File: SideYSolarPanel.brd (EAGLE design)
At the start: 81.7 x 102 mm, 33 parts

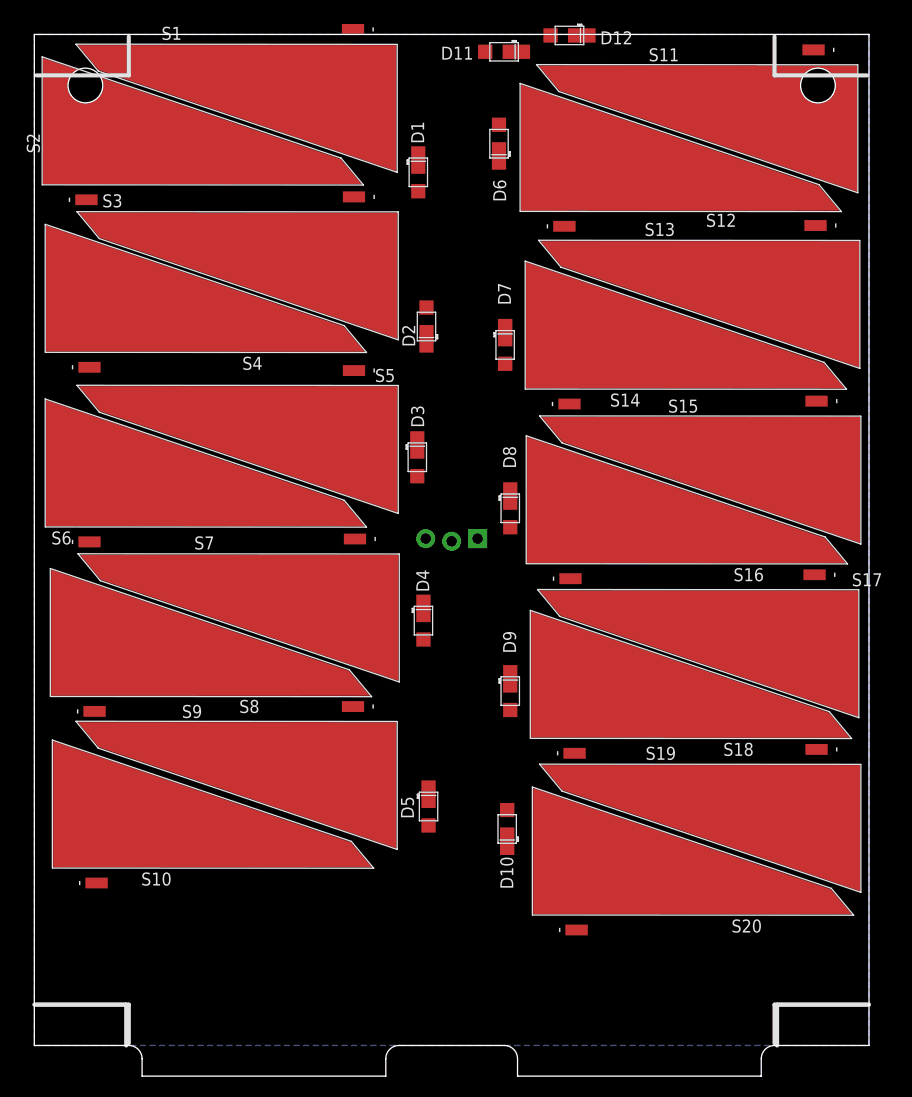
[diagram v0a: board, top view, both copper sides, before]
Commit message: Finished routing Y solar panel
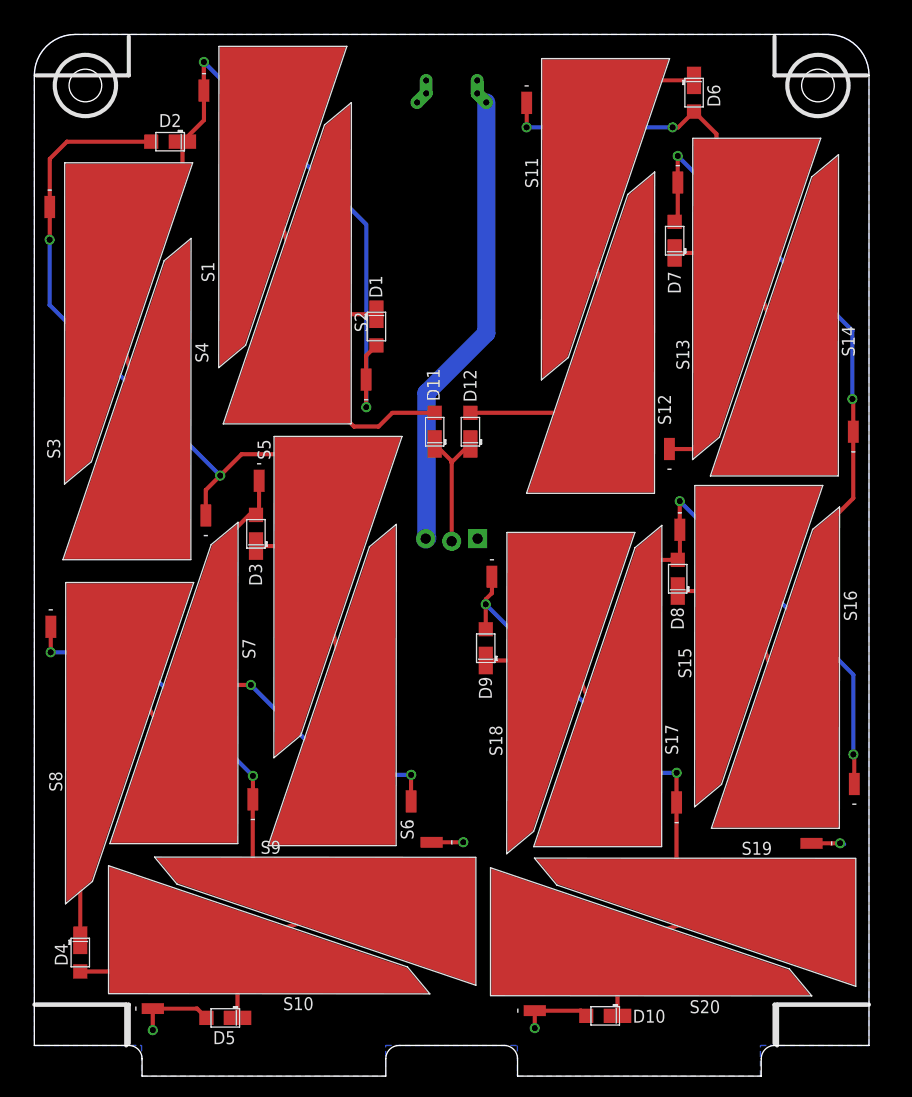
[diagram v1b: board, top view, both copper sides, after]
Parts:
- added U$1, U$2: BURNER, Burner:BURNER
- moved D4 46.7 mm to (4.50, 9.10)
- moved D12 40.0 mm to (42.7, 60.1), turned to 90 degrees
- moved D11 37.8 mm to (39.2, 60.1), turned to 90 degrees
- moved S6 36.1 mm to (35.3, 26.9), turned to 180 degrees
- moved D2 30.9 mm to (13.3, 88.5), turned to 180 degrees
- moved S16 29.8 mm to (78.7, 28.6), turned to 180 degrees
- moved D5 28.7 mm to (18.7, 2.70), turned to 180 degrees
- moved S2 28.0 mm to (30.9, 68.2), turned to 180 degrees
- moved S3 25.3 mm to (3.10, 79.1), turned to 0 degrees
- moved S11 24.4 mm to (49.8, 89.3), turned to 0 degrees
- moved S14 23.2 mm to (78.6, 63.1), turned to 180 degrees
- moved S7 22.6 mm to (19.8, 27.1), turned to 180 degrees
- moved S17 21.4 mm to (61.3, 26.8), turned to 180 degrees
- moved S12 21.2 mm to (60.6, 61.4), turned to 180 degrees
- moved D10 20.7 mm to (55.9, 2.90), turned to 180 degrees
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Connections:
- new net V_BURN: JP1.3, U$1.H1, U$1.H2, U$1.H3
- net GND: now also U$2.H1, U$2.H2, U$2.H3
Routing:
- net N$39: track 0.00 -> 119.4 mm, vias 0 -> 2
- net N$7: track 0.00 -> 107.4 mm, vias 0 -> 2
- net N$37: track 0.00 -> 103.9 mm, vias 0 -> 2
- net N$45: track 0.00 -> 103.4 mm, vias 0 -> 2
- net N$36: track 0.00 -> 97.9 mm, vias 0 -> 2
- net N$50: track 0.00 -> 96.5 mm, vias 0 -> 2
- net N$41: track 0.00 -> 86.1 mm, vias 0 -> 2
- net N$1: track 0.00 -> 86.0 mm, vias 0 -> 2
- net N$5: track 0.00 -> 66.1 mm
- net N$9: track 0.00 -> 53.3 mm
- net V_BURN: track 0.00 -> 45.2 mm
- net GND: track 0.00 -> 21.9 mm, vias 0 -> 4
- net V_SOLAR: track 0.00 -> 12.8 mm
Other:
- outline, holes or cut-outs redrawn

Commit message: Increased cutout line width
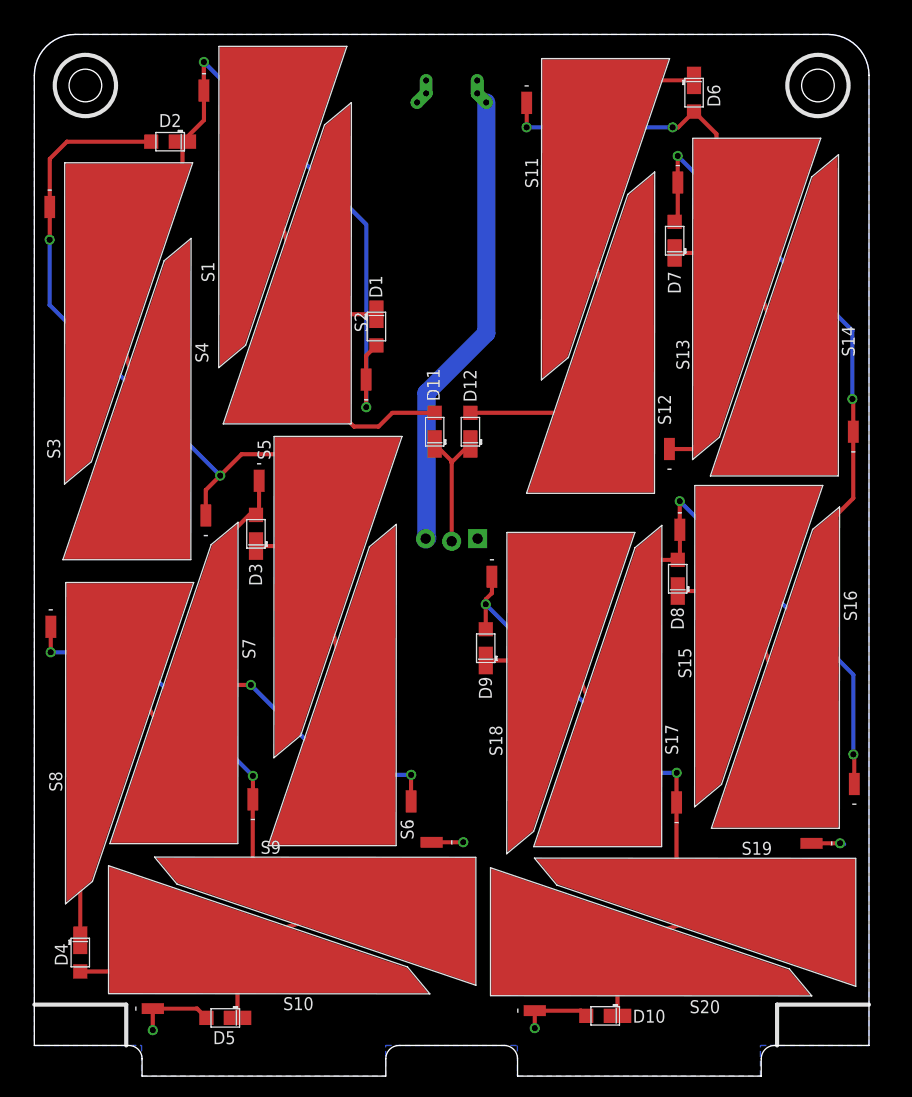
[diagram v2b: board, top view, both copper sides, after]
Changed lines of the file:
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@@
 <layer number="42" name="bRestrict" color="1" fill="10" visible="no" active="yes"/>
 <layer number="43" name="vRestrict" color="2" fill="10" visible="no" active="yes"/>
-<layer number="44" name="Drills" color="7" fill="1" visible="yes" active="yes"/>
-<layer number="45" name="Holes" color="7" fill="1" visible="yes" active="yes"/>
+<layer number="44" name="Drills" color="7" fill="1" visible="no" active="yes"/>
+<layer number="45" name="Holes" color="7" fill="1" visible="no" active="yes"/>
 <layer number="46" name="Milling" color="3" fill="1" visible="no" active="yes"/>
 <layer number="47" name="Measures" color="7" fill="1" visible="no" active="yes"/>
@@
 <layer number="113" name="IDFDebug" color="4" fill="1" visible="no" active="yes"/>
 <layer number="116" name="Patch_BOT" color="9" fill="4" visible="no" active="yes"/>
-<layer number="121" name="_tsilk" color="7" fill="1" visible="no" active="yes"/>
-<layer number="122" name="_bsilk" color="7" fill="1" visible="no" active="yes"/>
+<layer number="121" name="_tsilk" color="7" fill="1" visible="yes" active="yes"/>
+<layer number="122" name="_bsilk" color="7" fill="1" visible="yes" active="yes"/>
 <layer number="123" name="tTestmark" color="7" fill="1" visible="no" active="yes"/>
 <layer number="124" name="bTestmark" color="7" fill="1" visible="no" active="yes"/>
@@
 <wire x1="46.015" y1="0" x2="47.315" y2="-1.3" width="0" layer="20" curve="-90"/>
 <wire x1="71.18" y1="-1.3" x2="72.48" y2="0" width="0" layer="20" curve="-90"/>
-<wire x1="0.2" y1="4" x2="9.25" y2="4" width="0.4" layer="121"/>
-<wire x1="9.25" y1="4" x2="9.25" y2="0.2" width="0.4" layer="121"/>
-<wire x1="81.53" y1="94.99" x2="72.48" y2="94.99" width="0.4" layer="121"/>
-<wire x1="72.48" y1="94.99" x2="72.48" y2="98.79" width="0.4" layer="121"/>
-<wire x1="0.2" y1="94.99" x2="9.25" y2="94.99" width="0.4" layer="121"/>
-<wire x1="9.25" y1="94.99" x2="9.25" y2="98.79" width="0.4" layer="121"/>
-<wire x1="81.53" y1="4" x2="72.48" y2="4" width="0.4" layer="121"/>
-<wire x1="72.48" y1="4" x2="72.48" y2="0.2" width="0.4" layer="121"/>
-<rectangle x1="13.1" y1="58.8" x2="28.9" y2="77.8" layer="122"/>
 <hole x="5" y="94" drill="3.2"/>
 <hole x="76.73" y="94" drill="3.2"/>

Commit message: Swapped X and Y solar panels per NanoRacks ICD
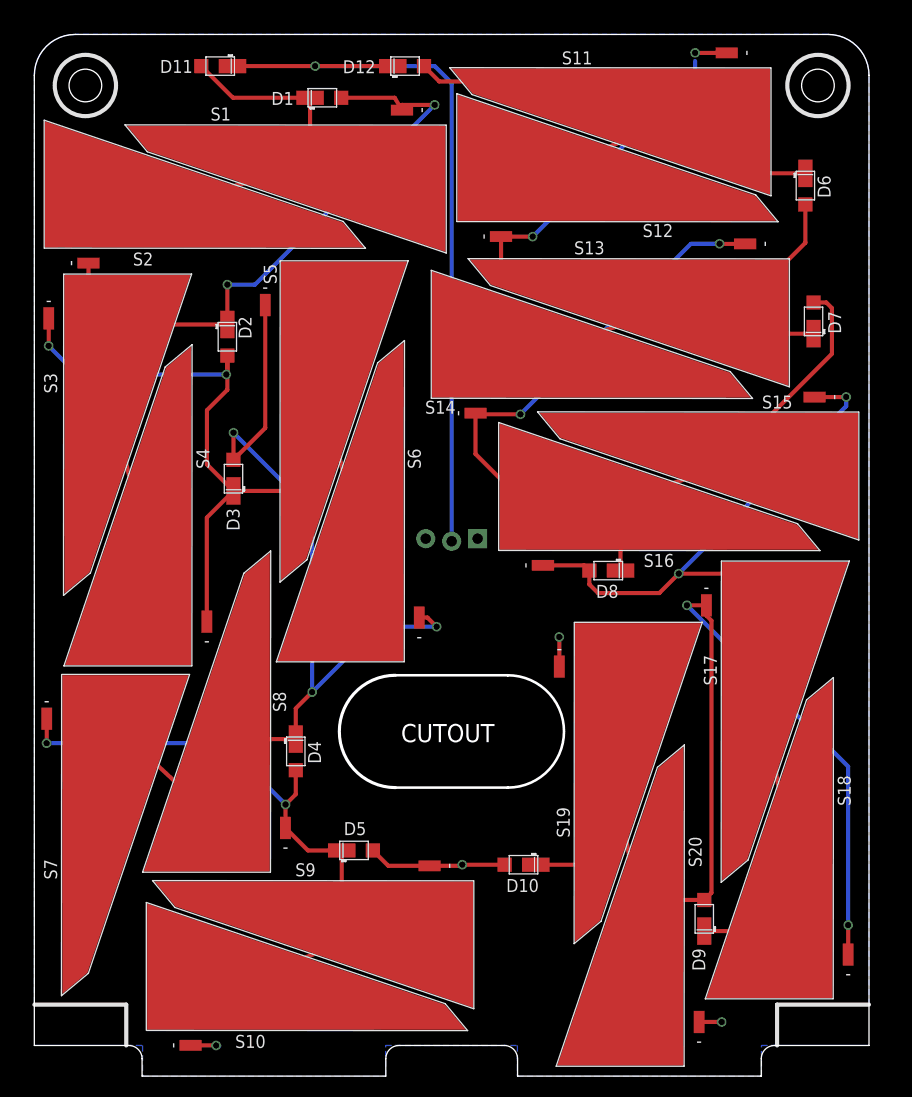
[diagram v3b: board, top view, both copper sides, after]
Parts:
- removed U$1, U$2: BURNER, Burner:BURNER
- moved S18 44.3 mm to (78.1, 11.9), turned to 180 degrees
- moved D11 41.5 mm to (18.2, 95.9), turned to 180 degrees
- moved D12 36.4 mm to (36.3, 95.9), turned to 0 degrees
- moved D9 34.1 mm to (65.6, 12.4)
- moved S16 32.7 mm to (52.8, 48.6), turned to 90 degrees
- moved S14 32.4 mm to (46.2, 63.5), turned to 90 degrees
- moved D4 28.9 mm to (25.6, 28.8)
- moved S19 25.6 mm to (53.0, 34.1), turned to 0 degrees
- moved S2 24.7 mm to (8.30, 78.2), turned to 90 degrees
- moved S8 24.1 mm to (23.0, 24.3), turned to 180 degrees
- moved D1 23.0 mm to (28.2, 92.8), turned to 0 degrees
- moved S12 22.8 mm to (48.7, 80.8), turned to 90 degrees
- moved D5 20.7 mm to (31.3, 19.1), turned to 0 degrees
- moved D2 19.9 mm to (18.9, 69.4), turned to 270 degrees
- moved S6 18.0 mm to (36.1, 44.9)
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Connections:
- removed net V_BURN: JP1.3, U$1.H1, U$1.H2, U$1.H3
- net GND: no longer U$2.H1, U$2.H2, U$2.H3
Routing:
- net V_SOLAR: track 12.8 -> 74.6 mm, vias 0 -> 1
- net V_BURN: track 45.2 -> 0.00 mm
- net N$41: track 86.1 -> 128.2 mm
- net N$50: track 96.5 -> 79.2 mm
- net N$39: track 119.4 -> 104.1 mm, vias 2 -> 3
- net N$1: track 86.0 -> 97.7 mm
- net N$5: track 66.1 -> 76.4 mm
- net N$45: track 103.4 -> 95.6 mm
- net N$37: track 103.9 -> 99.6 mm
- net N$9: track 53.3 -> 54.5 mm
- net N$7: track 107.4 -> 108.5 mm
- net GND: track 21.9 -> 22.9 mm
- net N$36: track 97.9 -> 98.5 mm
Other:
- outline, holes or cut-outs redrawn
- board text added: "CUTOUT"

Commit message: Cleanup
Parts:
- added FRAME1: FRAME-LETTER, SparkFun-Aesthetics:CREATIVE_COMMONS
- added U$1: KICKSAT_LOGO, KickSat-Logo:KICKSAT_LOGO
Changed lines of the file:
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@@
 </element>
 <element name="JP1" library="SparkFun-Connectors" package="MOLEX-1X3_LOCK" value="" x="43.405" y="49.5" rot="MR0"/>
+<element name="FRAME1" library="SparkFun-Aesthetics" package="CREATIVE_COMMONS" value="FRAME-LETTER" x="20.8" y="-10.6"/>
+<element name="U$1" library="KickSat-Logo" package="KICKSAT_LOGO" value="KICKSAT_LOGO" x="54.2" y="2.8" rot="MR0"/>
 </elements>
 <signals>

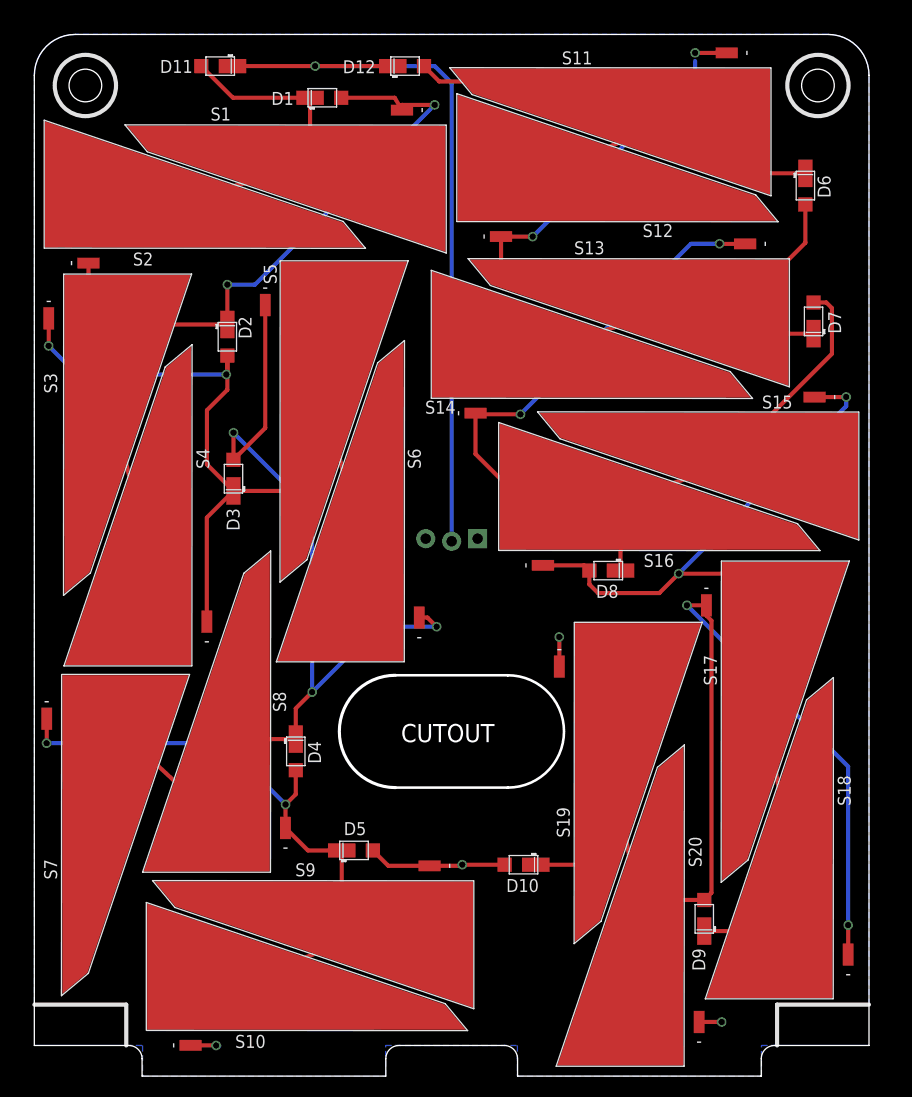
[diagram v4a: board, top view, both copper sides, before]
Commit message: Fixed solar cell footprints
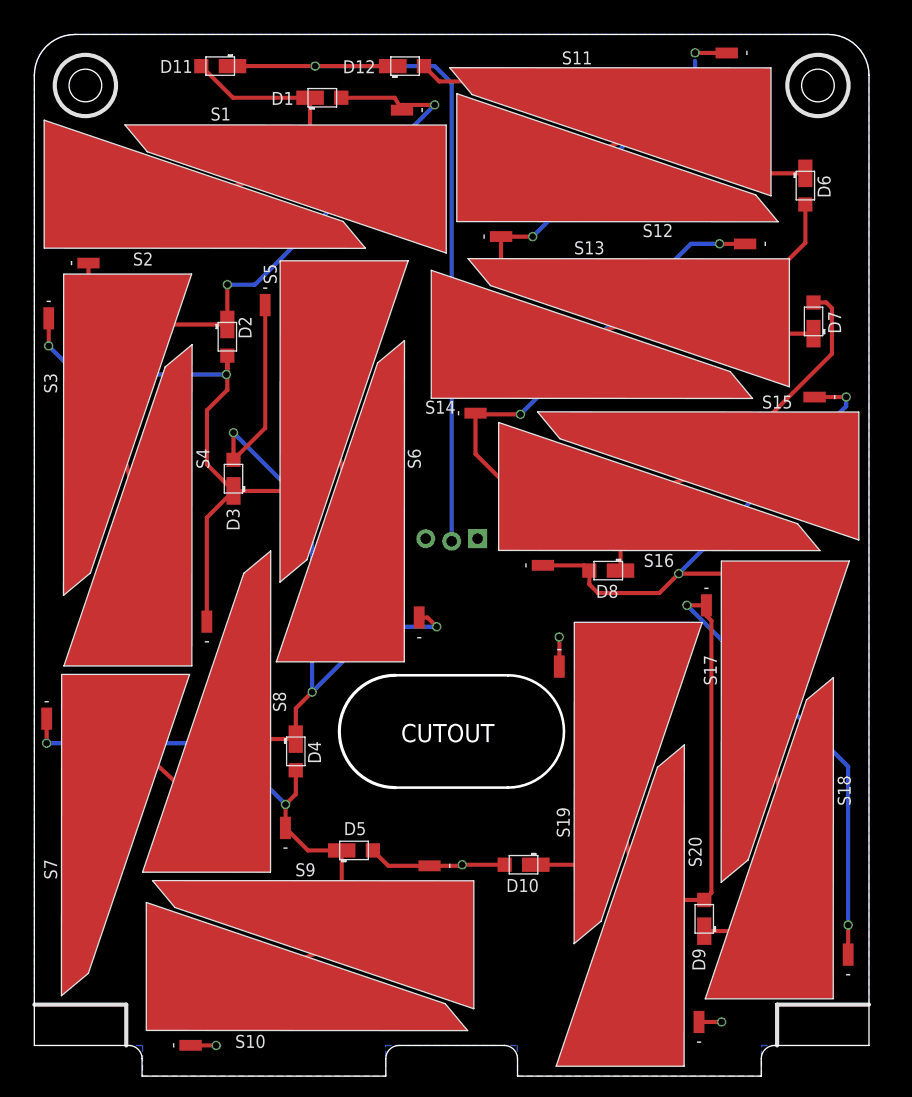
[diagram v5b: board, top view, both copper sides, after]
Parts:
- D1, D10, D11, D12, D2, D3, D4, D5, D6, D7, D8, D9: device phonesat:SB_DIODE -> Solar:SB_DIODE
- S1, S10, S11, S12, S13, S14, S15, S16, S17, S18, S19, S2, S20, S3, S4, S5, S6, S7, S8, S9: device phonesat:SOLAR_CELL -> Solar:SOLAR_CELL
